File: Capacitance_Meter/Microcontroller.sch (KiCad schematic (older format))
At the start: 1 part

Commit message: USB library and footprint
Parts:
- STM32: footprint (none) -> STM32_Dev_Boards:STM32F411CEU6
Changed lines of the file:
@@
 F 0 "STM32" H 5450 5515 50  0000 C CNN
 F 1 "STM32F411CEU6" H 5450 5424 50  0000 C CNN
-F 2 "" H 5500 4450 50  0001 C CNN
+F 2 "STM32_Dev_Boards:STM32F411CEU6" H 5500 4450 50  0001 C CNN
 F 3 "" H 5500 4450 50  0001 C CNN
 	1    5450 3850

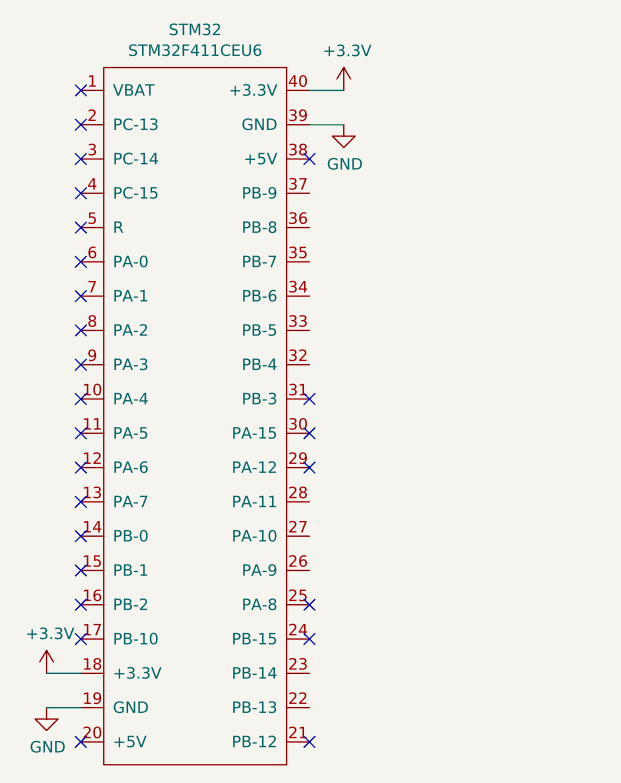
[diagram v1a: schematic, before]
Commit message: Update to capacitance meter
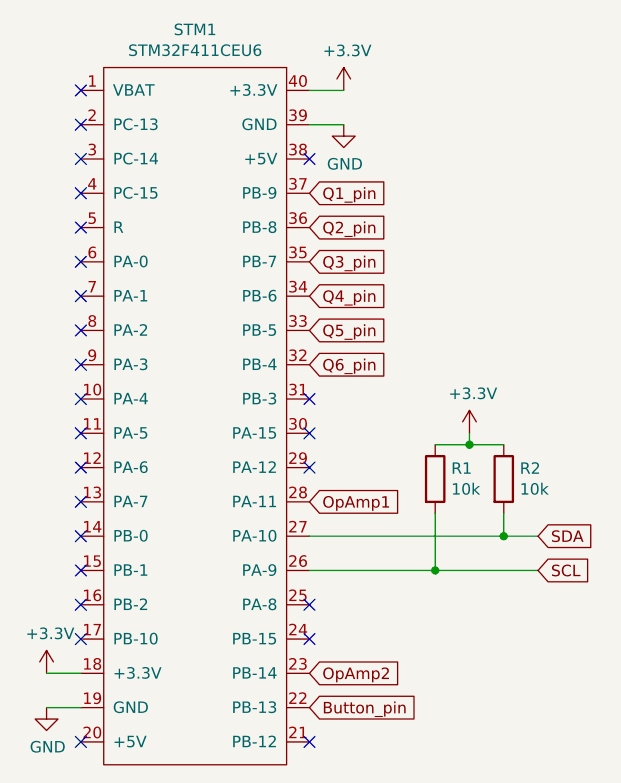
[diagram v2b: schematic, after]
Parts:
- removed STM32: STM32F411CEU6, STM32_Dev_Boards:STM32F411CEU6, symbol STM32_Dev_Boards:STM32F411CEU6
- added R1, R2: 10k, Resistor_SMD:R_0805_2012Metric, symbol Device:R
- added STM1: STM32F411CEU6, STM32_Dev_Boards:STM32F411CEU6, symbol STM32_Dev_Boards:STM32F411CEU6
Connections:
- net +3V3: now also R1.1, R2.1, STM1.18 (+3.3V), STM1.40 (+3.3V)
- net GND: now also STM1.19 (GND), STM1.39 (GND)
- new net Button_pin: STM1.22 (PB-13)
- new net OpAmp1: STM1.28 (PA-11)
- new net OpAmp2: STM1.23 (PB-14)
- new net Q1_pin: STM1.37 (PB-9)
- new net Q2_pin: STM1.36 (PB-8)
- new net Q3_pin: STM1.35 (PB-7)
- new net Q4_pin: STM1.34 (PB-6)
- new net Q5_pin: STM1.33 (PB-5)
- new net Q6_pin: STM1.32 (PB-4)
- new net SCL: R1.2, STM1.26 (PA-9)
- new net SDA: R2.2, STM1.27 (PA-10)
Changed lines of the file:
@@
 $Descr A4 11693 8268
 encoding utf-8
-Sheet 3 3
+Sheet 3 5
 Title ""
 Date ""
@@
 Comment4 ""
 $EndDescr
-$Comp
-L STM32_Dev_Boards:STM32F411CEU6 STM32
-U 1 1 5ECA77B9
-P 5450 3850
-F 0 "STM32" H 5450 5515 50  0000 C CNN
-F 1 "STM32F411CEU6" H 5450 5424 50  0000 C CNN
-F 2 "STM32_Dev_Boards:STM32F411CEU6" H 5500 4450 50  0001 C CNN
-F 3 "" H 5500 4450 50  0001 C CNN
-	1    5450 3850
-	1    0    0    -1
-$EndComp
 NoConn ~ 4950 2450
 NoConn ~ 4950 2600
@@
 	4800 5150 4950 5150
 Wire Wire Line
+	5950 2600 6100 2600
+Wire Wire Line
 	5950 2450 6100 2450
+Text GLabel 5950 2900 2    50   Input ~ 0
+Q1_pin
+Text GLabel 5950 3050 2    50   Input ~ 0
+Q2_pin
+Text GLabel 5950 3200 2    50   Input ~ 0
+Q3_pin
+Text GLabel 5950 3350 2    50   Input ~ 0
+Q4_pin
+Text GLabel 5950 3500 2    50   Input ~ 0
+Q5_pin
+Text GLabel 5950 3650 2    50   Input ~ 0
+Q6_pin
+Text GLabel 5950 4250 2    50   Input ~ 0
+OpAmp1
+Text GLabel 5950 5000 2    50   Input ~ 0
+OpAmp2
+Text GLabel 5950 5150 2    50   Input ~ 0
+Button_pin
+Text GLabel 6950 4400 2    50   Input ~ 0
+SDA
+Text GLabel 6950 4550 2    50   Input ~ 0
+SCL
+$Comp
+L Device:R R2
+U 1 1 5EDCDB8B
+P 6800 4150
+F 0 "R2" H 6870 4196 50  0000 L CNN
+F 1 "10k" H 6870 4105 50  0000 L CNN
+F 2 "Resistor_SMD:R_0805_2012Metric" V 6730 4150 50  0001 C CNN
+F 3 "~" H 6800 4150 50  0001 C CNN
+	1    6800 4150
+	1    0    0    -1
+$EndComp
+$Comp
+L Device:R R1
+U 1 1 5EDCECA1
+P 6500 4150
+F 0 "R1" H 6570 4196 50  0000 L CNN
+F 1 "10k" H 6570 4105 50  0000 L CNN
+F 2 "Resistor_SMD:R_0805_2012Metric" V 6430 4150 50  0001 C CNN
+F 3 "~" H 6500 4150 50  0001 C CNN
+	1    6500 4150
+	1    0    0    -1
+$EndComp
 Wire Wire Line
-	5950 2600 6100 2600
+	6500 4300 6500 4550
+Wire Wire Line
+	6500 4550 6950 4550
+$Comp
+L power:+3.3V #PWR01
+U 1 1 5EDD1C38
+P 6650 3950
+F 0 "#PWR01" H 6650 3800 50  0001 C CNN
+F 1 "+3.3V" H 6665 4123 50  0000 C CNN
+F 2 "" H 6650 3950 50  0001 C CNN
+F 3 "" H 6650 3950 50  0001 C CNN
+	1    6650 3950
+	1    0    0    -1
+$EndComp
+Wire Wire Line
+	6800 4300 6800 4400
+Wire Wire Line
+	6800 4400 6950 4400
+Wire Wire Line
+	6500 4000 6650 4000
+Wire Wire Line
+	6650 4000 6650 3950
+Connection ~ 6650 4000
+Wire Wire Line
+	6650 4000 6800 4000
+Wire Wire Line
+	5950 4400 6800 4400
+Connection ~ 6800 4400
+Wire Wire Line
+	5950 4550 6500 4550
+Connection ~ 6500 4550
+$Comp
+L STM32_Dev_Boards:STM32F411CEU6 STM1
+U 1 1 5EDCD317
+P 5450 3850
+F 0 "STM1" H 5450 5515 50  0000 C CNN
+F 1 "STM32F411CEU6" H 5450 5424 50  0000 C CNN
+F 2 "STM32_Dev_Boards:STM32F411CEU6" H 5500 4450 50  0001 C CNN
+F 3 "" H 5500 4450 50  0001 C CNN
+	1    5450 3850
+	1    0    0    -1
+$EndComp
 $EndSCHEMATC
